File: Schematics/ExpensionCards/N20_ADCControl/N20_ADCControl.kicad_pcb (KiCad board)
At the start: 2 copper layers, 96.5 x 62 mm, 36 parts

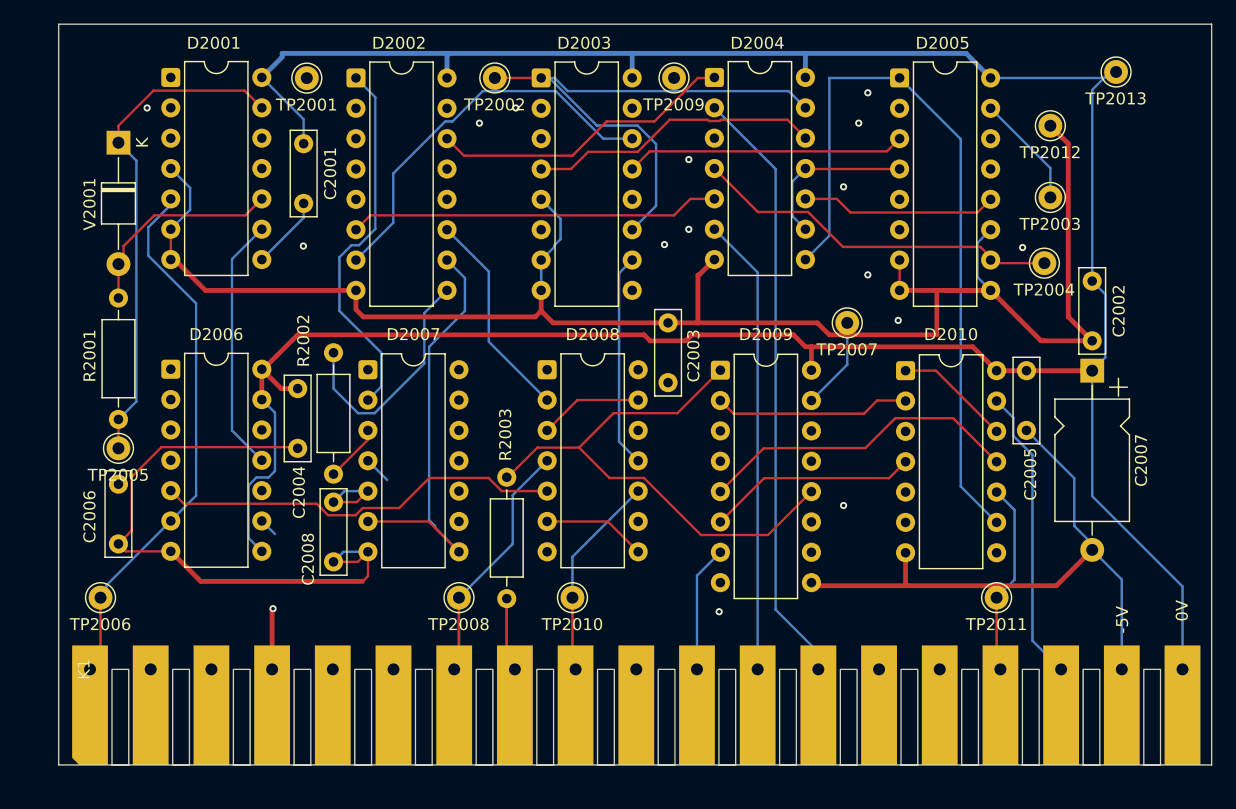
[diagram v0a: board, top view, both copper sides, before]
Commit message: Reworked N20/N21
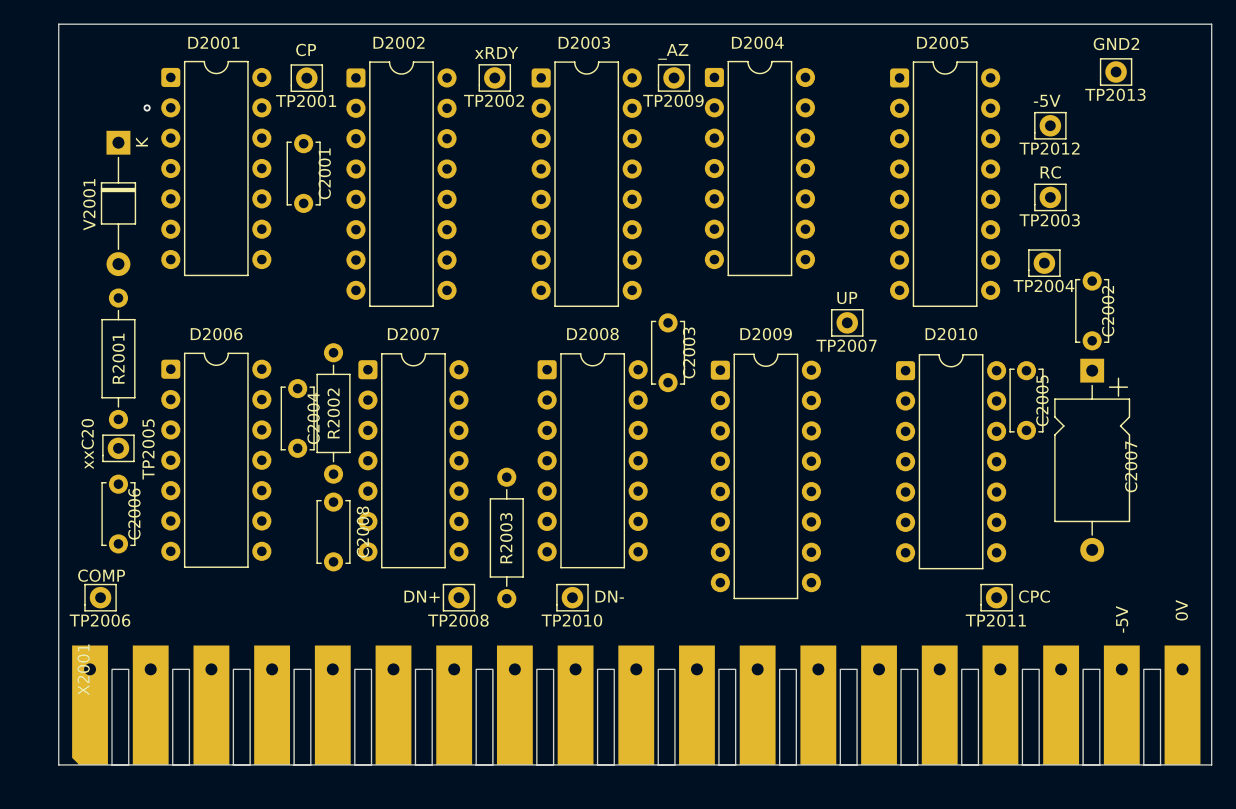
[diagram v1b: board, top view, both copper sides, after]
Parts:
- C2001, C2002, C2003, C2004, C2005, C2006, C2008: footprint Capacitor_THT:C_Rect_L7.0mm_W2.0mm_P5.00mm -> Capacitor_THT:C_Disc_D5.0mm_W2.5mm_P5.00mm
- TP2001, TP2002, TP2003, TP2004, TP2005, TP2006, TP2007, TP2008, TP2009, TP2010, TP2011, TP2012, TP2013: footprint Connector_Pin:Pin_D1.0mm_L10.0mm -> Connector_Pin:Pin_D0.9mm_L10.0mm_W2.4mm_FlatFork
- renumbered K1 to X2001
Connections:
- net /_C20 renamed /xxC20
- net /_EC20 renamed /xEC20
- net /_ECP renamed /xECP
- net /_ENC20 renamed /xENC20
- net /_ERD renamed /xERD
- net /_RDY renamed /xRDY
- net /_SCP renamed /xSCP
- net /_STD renamed /xSTD
- net /~{CP} renamed /x~{CP}
- net /~{_RD} renamed /x~{RD}
- D2002 pad 15: /_AZ -> /xAZ
- D2003 pad 12: /AZ -> /xAZ
- D2009 pad 1: /_AZ -> /xAZ
- D2009 pad 12: /_AZ -> /xAZ
- R2003 pad 1: /_AZ -> /xAZ
- TP2009 pad 1: /_AZ -> /xAZ
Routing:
- net -5V: track 255.6 -> 0.00 mm
- net GND2: track 237.3 -> 0.00 mm
- net /xECP: track 93.6 -> 0.00 mm
- net /xxC20: track 78.0 -> 0.00 mm
- net /COMP: track 50.6 -> 0.00 mm
- net /HSM: track 50.6 -> 0.00 mm
- net /SRUP: track 48.1 -> 0.00 mm
- net /xRDY: track 46.9 -> 0.00 mm
- net /_AZ: track 45.6 -> 0.00 mm
- net /SAZ: track 35.2 -> 0.00 mm
- net /RC: track 34.2 -> 0.00 mm
- net /POL: track 34.1 -> 0.00 mm
- net /x~{RD}: track 33.0 -> 0.00 mm
- net /xSTD: track 31.1 -> 0.00 mm
- net Net-(D2005B-J): track 30.7 -> 0.00 mm
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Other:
- board text added: "-5V"
- board text added: "COMP"
- board text added: "CP"
- board text added: "CPC"
- board text added: "DN+"
- board text added: "DN-"
- board text added: "GND2"
- board text added: "RC"
- board text added: "UP"
- board text added: "_AZ"
- board text added: "xRDY"
- board text added: "xxC20"

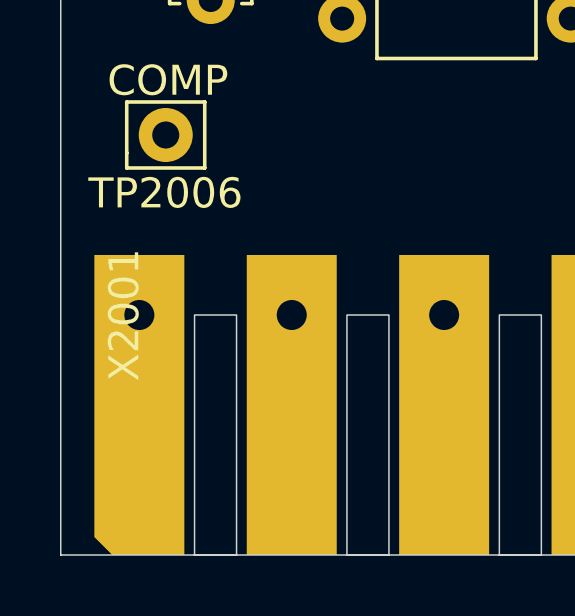
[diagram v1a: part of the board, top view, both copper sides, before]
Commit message: Small modifications, more disassembly
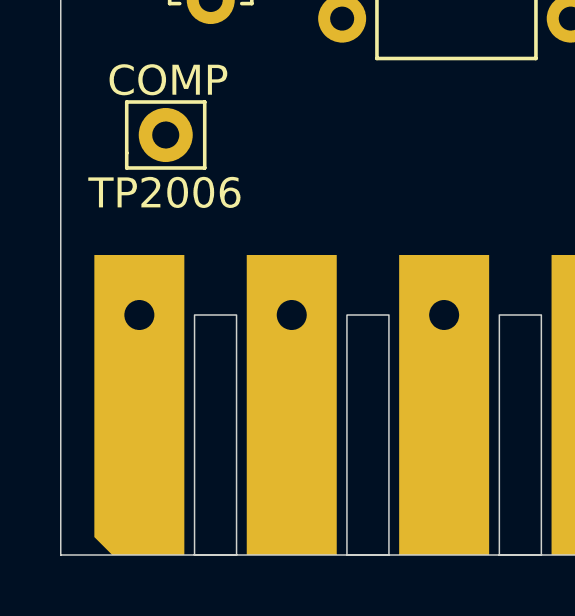
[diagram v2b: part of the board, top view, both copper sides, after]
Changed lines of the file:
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@@
 			(unlocked yes)
 			(layer "F.SilkS")
+			(hide yes)
 			(effects
 				(font

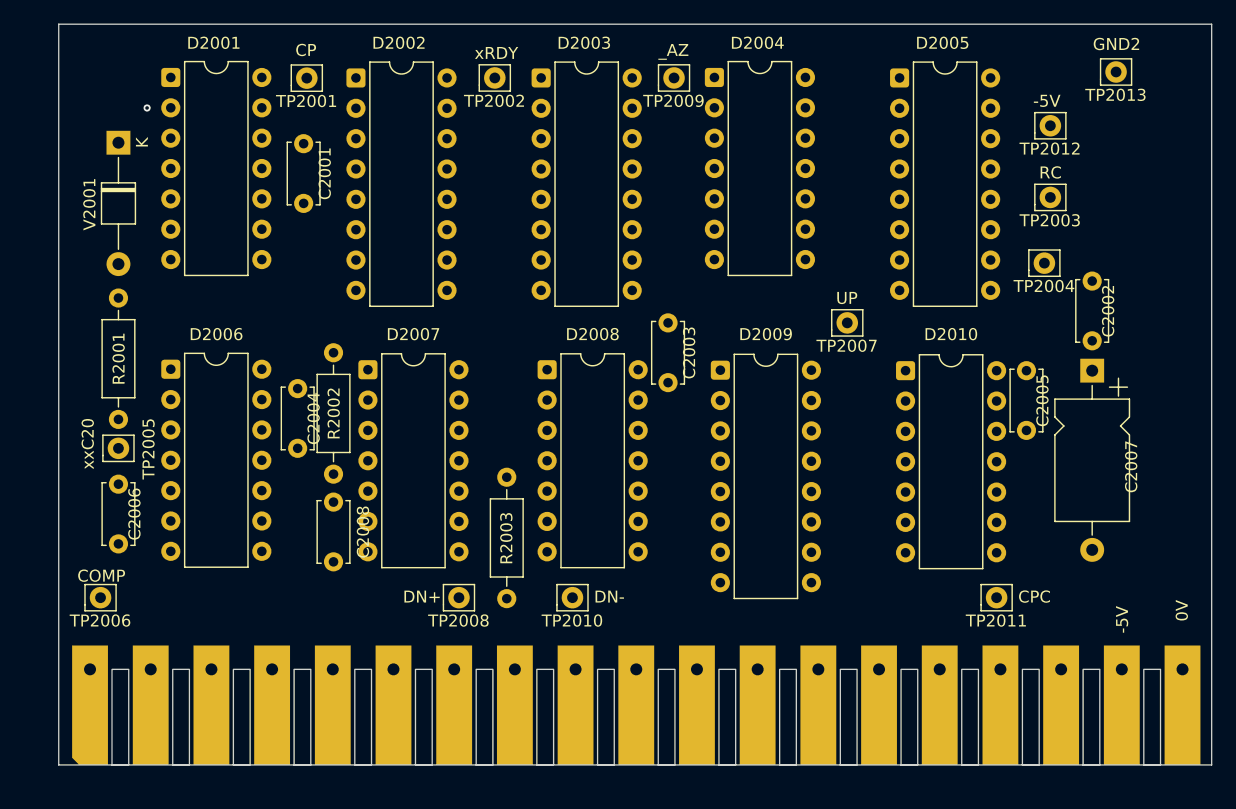
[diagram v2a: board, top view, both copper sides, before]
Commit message: Some more disassembly, optimize N20 schematics (naming of signals)
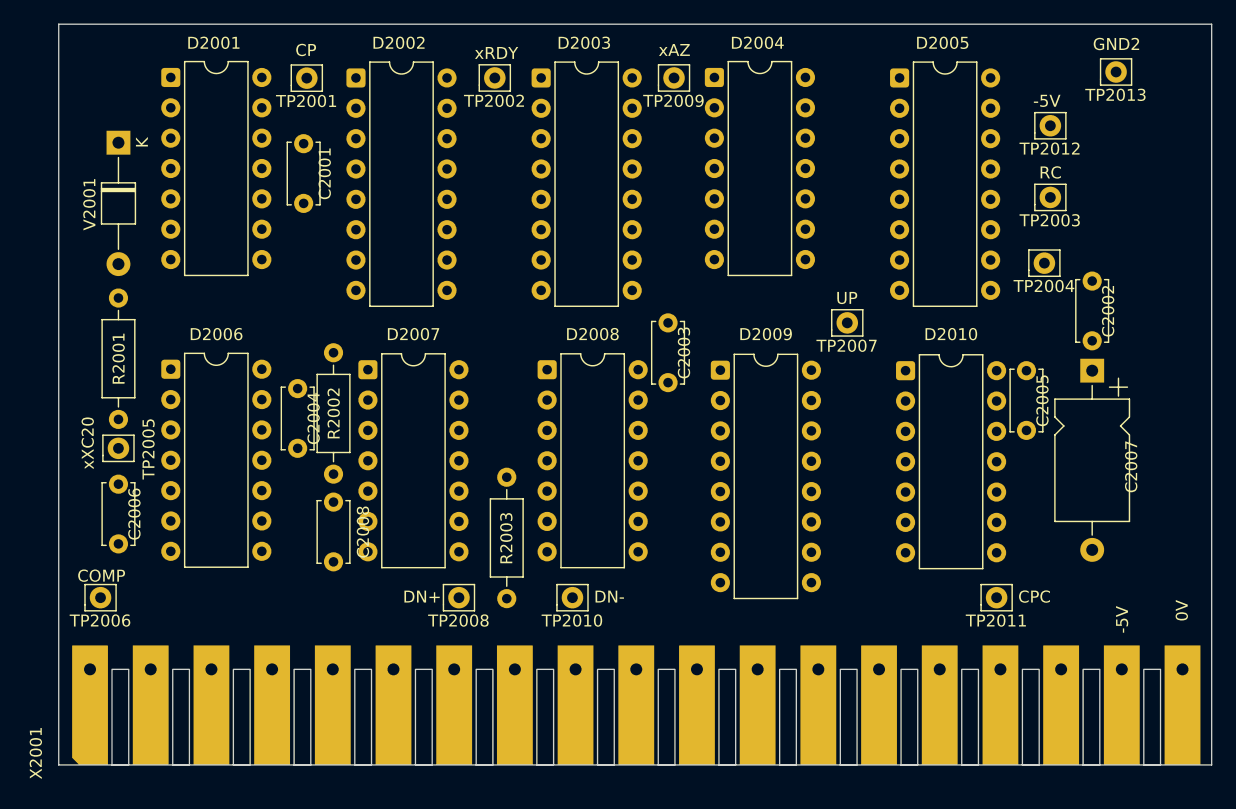
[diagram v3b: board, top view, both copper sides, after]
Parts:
- R2003: value 1k0 -> 1k00
- X2001: footprint PM2528:PM2528_RiserCardConnector -> Philips_PM2528:PM2528_RiserCardConnector
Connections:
- net /xxC20 renamed /xXC20
- net /~{UP} renamed /x~{UP}
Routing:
- net (no net): vias 1 -> 0
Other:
- board text added: "xAZ"
- board text added: "xXC20"
- board text removed: "_AZ"
- board text removed: "xxC20"
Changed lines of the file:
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@@
 	(title_block
 		(title "Philips PM2528 - N20 (ADC Control)")
-		(date "2025-08-07")
+		(date "2025-09-12")
 		(rev "1.0")
 		(company "D. Kupers")
@@
 	(net 28 "unconnected-(D2002B-Q2-Pad12)")
 	(net 29 "unconnected-(D2002A-Q3-Pad5)")
-	(net 30 "/xxC20")
+	(net 30 "/xXC20")
 	(net 31 "/xAZ")
 	(net 32 "unconnected-(D2002A-Q1-Pad3)")
@@
 	(net 53 "Net-(D2007-Pad3)")
 	(net 54 "unconnected-(D2007-Pad11)")
-	(net 55 "/~{UP}")
+	(net 55 "/x~{UP}")
 	(net 56 "unconnected-(D2007-Pad13)")
 	(net 57 "/xENC20")
@@
 			(layers "*.Cu" "*.Mask")
 			(remove_unused_layers no)
-			(net 30 "/xxC20")
+			(net 30 "/xXC20")
 			(pinfunction "Q")
 			(pintype "output")
@@
 			(layers "*.Cu" "*.Mask")
 			(remove_unused_layers no)
-			(net 30 "/xxC20")
+			(net 30 "/xXC20")
 			(pinfunction "Enable")
 			(pintype "input")
@@
 			(layers "*.Cu" "*.Mask")
 			(remove_unused_layers no)
-			(net 55 "/~{UP}")
+			(net 55 "/x~{UP}")
 			(pinfunction "~{Q}")
 			(pintype "output")
@@
 			(layers "*.Cu" "*.Mask")
 			(remove_unused_layers no)
-			(net 55 "/~{UP}")
+			(net 55 "/x~{UP}")
 			(pintype "input")
 		)
@@
 			(layers "*.Cu" "*.Mask")
 			(remove_unused_layers no)
-			(net 30 "/xxC20")
+			(net 30 "/xXC20")
 			(pintype "passive")
 		)
@@
 			(layers "*.Cu" "*.Mask")
 			(remove_unused_layers no)
-			(net 30 "/xxC20")
+			(net 30 "/xXC20")
 			(pinfunction "K")
 			(pintype "passive")
@@
 			(remove_unused_layers no)
 			(roundrect_rratio 0.15625)
-			(net 55 "/~{UP}")
+			(net 55 "/x~{UP}")
 			(pintype "input")
 		)
@@
 			(layers "*.Cu" "*.Mask")
 			(remove_unused_layers no)
-			(net 30 "/xxC20")
+			(net 30 "/xXC20")
 			(pintype "input")
 		)
@@
 			(layers "*.Cu" "*.Mask")
 			(remove_unused_layers no)
-			(net 30 "/xxC20")
+			(net 30 "/xXC20")
 			(pintype "input")
 		)
@@
 			)
 		)
-		(property "Value" "1k0"
+		(property "Value" "1k00"
 			(at 5.08 2.37 90)
 			(layer "F.Fab")
@@
 		)
 	)
-	(footprint "PM2528:PM2528_RiserCardConnector"
+	(footprint "Philips_PM2528:PM2528_RiserCardConnector"
 		(layer "F.Cu")
 		(at 104.57 125.22 90)
 		(property "Reference" "X2001"
-			(at 0 -0.5 90)
+			(at -7 -4.5 90)
 			(unlocked yes)
 			(layer "F.SilkS")
-			(hide yes)
 			(effects
 				(font
@@
 		)
 		(property "Value" "~"
-			(at 0 1 90)
+			(at -0.5 -3 90)
 			(unlocked yes)
 			(layer "F.Fab")
@@
 		)
 		(fp_text user "${REFERENCE}"
-			(at 0 2.5 90)
+			(at 5 -4.5 90)
 			(unlocked yes)
 			(layer "F.Fab")
@@
 			(layers "*.Cu" "*.Mask")
 			(remove_unused_layers no)
-			(net 30 "/xxC20")
+			(net 30 "/xXC20")
 			(pinfunction "1")
 			(pintype "passive")
@@
 		(tags "C Disc series Radial pin pitch 5.00mm diameter 5mm width 2.5mm Capacitor")
 		(property "Reference" "C2003"
-			(at 2.5 1.8 90)
+			(at 2.5 1.37 90)
 			(layer "F.SilkS")
 			(effects
@@
 		)
 	)
-	(gr_text "_AZ"
+	(gr_text "xAZ"
 		(at 152.15 74 0)
 		(layer "F.SilkS")
@@
 		)
 	)
-	(gr_text "xxC20"
+	(gr_text "xXC20"
 		(at 105 108.5 90)
 		(layer "F.SilkS")
@@
 		)
 	)
-	(via
-		(at 109.347 78.232)
-		(size 0.6)
-		(drill 0.3)
-		(layers "F.Cu" "B.Cu")
-		(net 0)
-	)
 	(embedded_fonts no)

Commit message: Small updates Some GPIB-analyzing-functions found.
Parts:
- X2001: footprint Philips_PM2528:PM2528_RiserCardConnector -> PhilipsPM2528:PM2528_RiserCardConnector
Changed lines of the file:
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@@
 	(title_block
 		(title "Philips PM2528 - N20 (ADC Control)")
-		(date "2025-09-12")
+		(date "2025-09-14")
 		(rev "1.0")
 		(company "D. Kupers")
@@
 		)
 	)
-	(footprint "Philips_PM2528:PM2528_RiserCardConnector"
+	(footprint "PhilipsPM2528:PM2528_RiserCardConnector"
 		(layer "F.Cu")
 		(at 104.57 125.22 90)
